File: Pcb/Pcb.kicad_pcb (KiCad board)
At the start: 2 copper layers, 152.3 x 104.7 mm, 133 parts, among them J1 TRRS, Q1 2N7002, SW1 SW_Push, SW10 SW_Push, SW11 SW_Push, SW12 SW_Push, SW13 SW_Push, SW14 SW_Push, SW15 SW_Push, SW16 SW_Push, SW17 SW_Push, SW18 SW_Push, SW19 SW_Push, SW2 SW2, SW20 SW_Push, SW21 SW_Push, SW22 SW_Push, SW23 SW_Push, SW24 SW_Push, SW25 SW_Push, SW26 SW_Push, SW27 SW_Push, SW28 SW_Push, SW29 SW_Push, SW3 SW_Push, SW4 SW_Push, SW5 SW_Push, SW6 SW_Push, SW7 SW_Push, SW8 SW_Push, SW9 SW_Push, U1 ProMicro

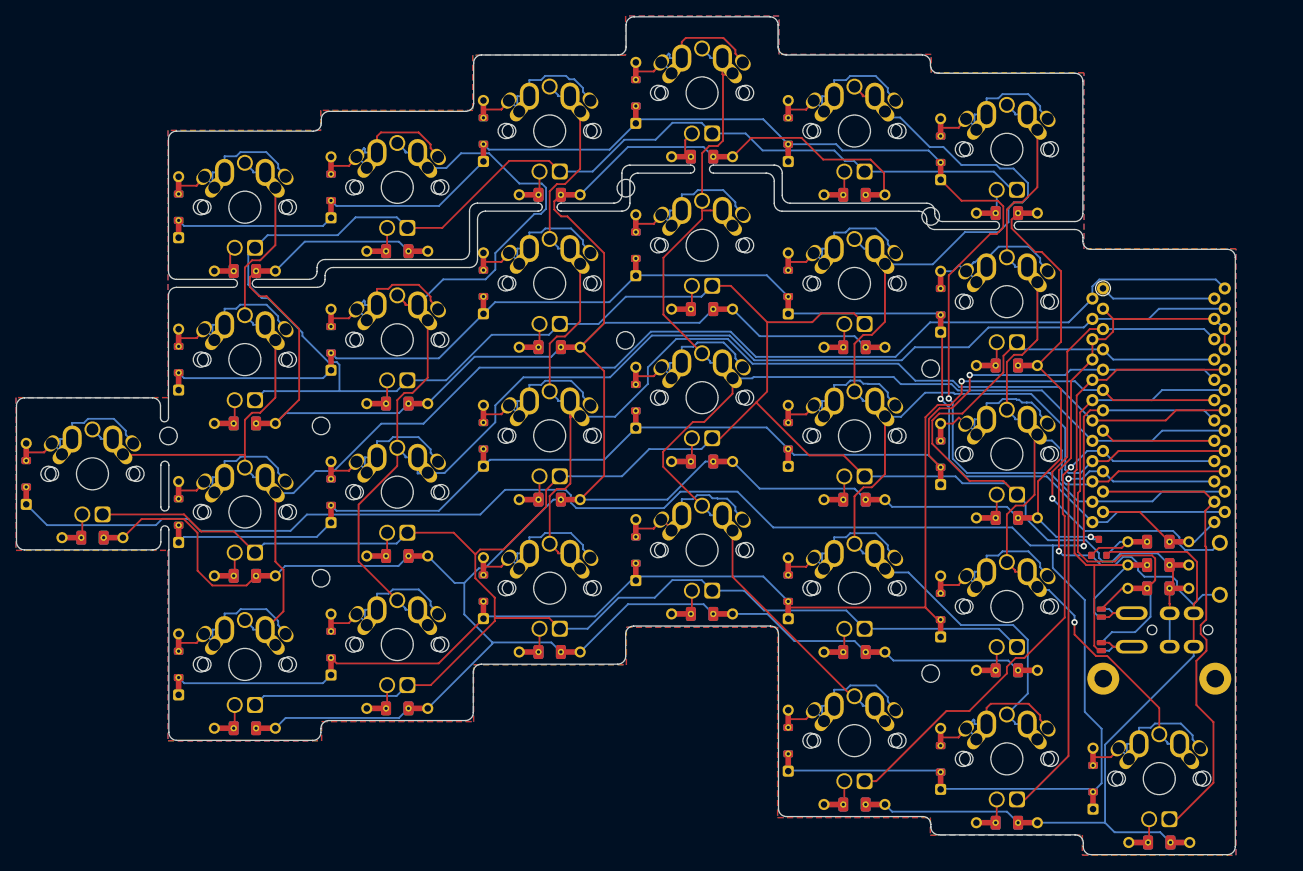
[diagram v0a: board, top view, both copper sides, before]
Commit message: Delete all tracks
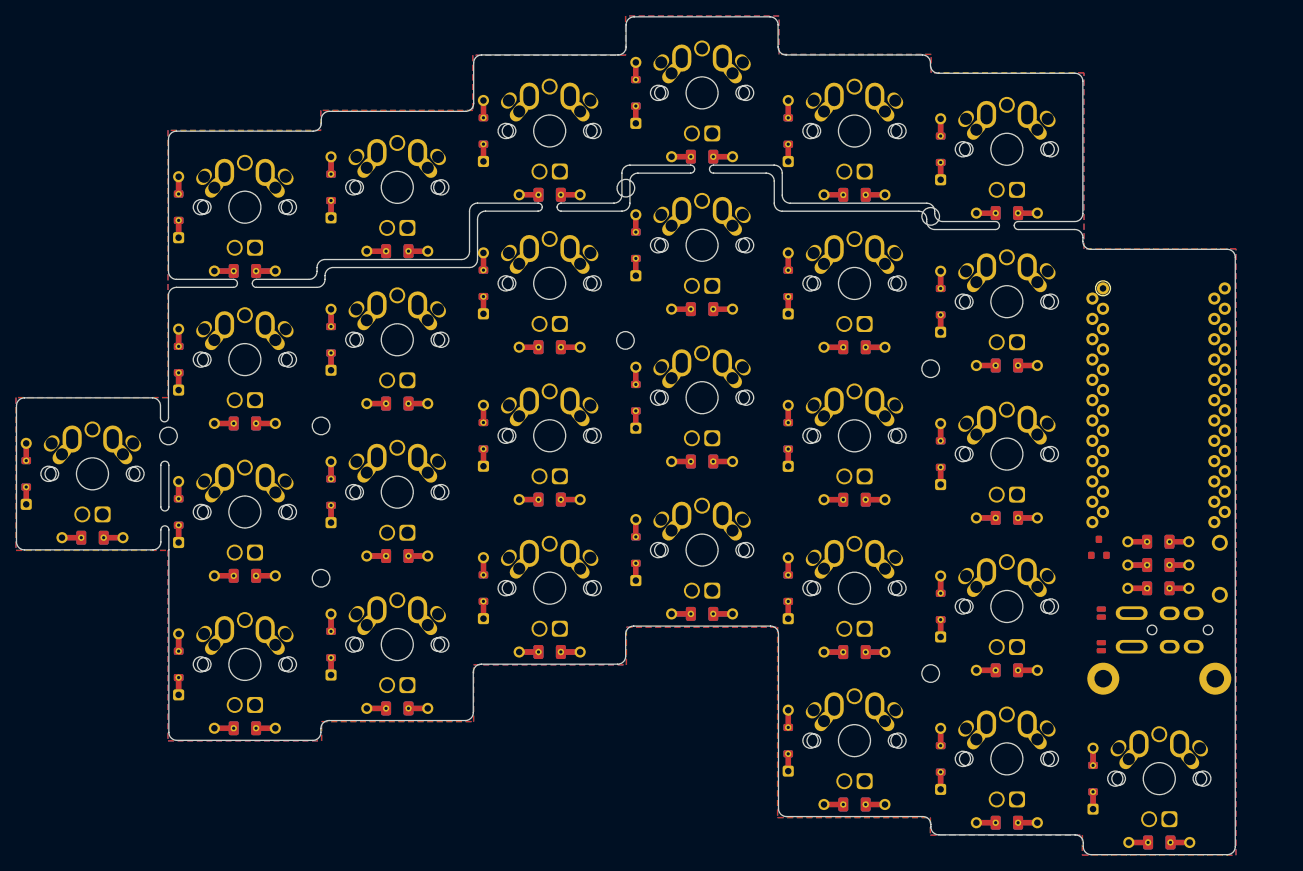
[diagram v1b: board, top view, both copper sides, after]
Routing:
- net VCC: track 572.4 -> 0.00 mm
- net /LEDOut: track 543.6 -> 0.00 mm, vias 1 -> 0
- net /rowE: track 255.7 -> 0.00 mm, vias 1 -> 0
- net /col0: track 231.3 -> 0.00 mm
- net /col1: track 218.4 -> 0.00 mm
- net /rowA: track 196.6 -> 0.00 mm, vias 1 -> 0
- net /col4: track 195.5 -> 0.00 mm
- net /col3: track 183.5 -> 0.00 mm
- net /rowD: track 179.1 -> 0.00 mm, vias 1 -> 0
- net GND: track 169.8 -> 0.00 mm, vias 1 -> 0
- net /rowB: track 169.5 -> 0.00 mm, vias 1 -> 0
- net /col2: track 167.3 -> 0.00 mm
- net /rowC: track 162.4 -> 0.00 mm, vias 1 -> 0
- net /col5: track 137.0 -> 0.00 mm, vias 1 -> 0
- net /CAPS: track 72.6 -> 0.00 mm, vias 1 -> 0
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
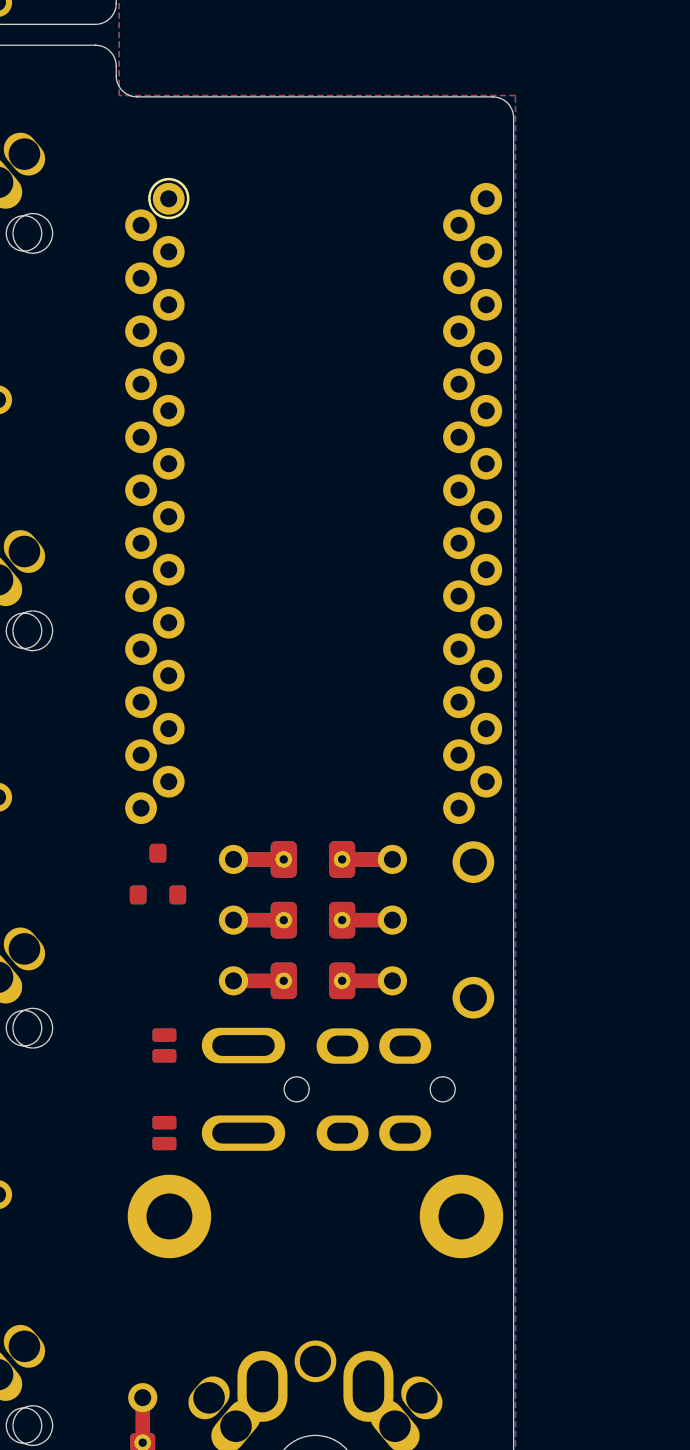
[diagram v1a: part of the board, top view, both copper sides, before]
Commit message: Remove I2C resistors
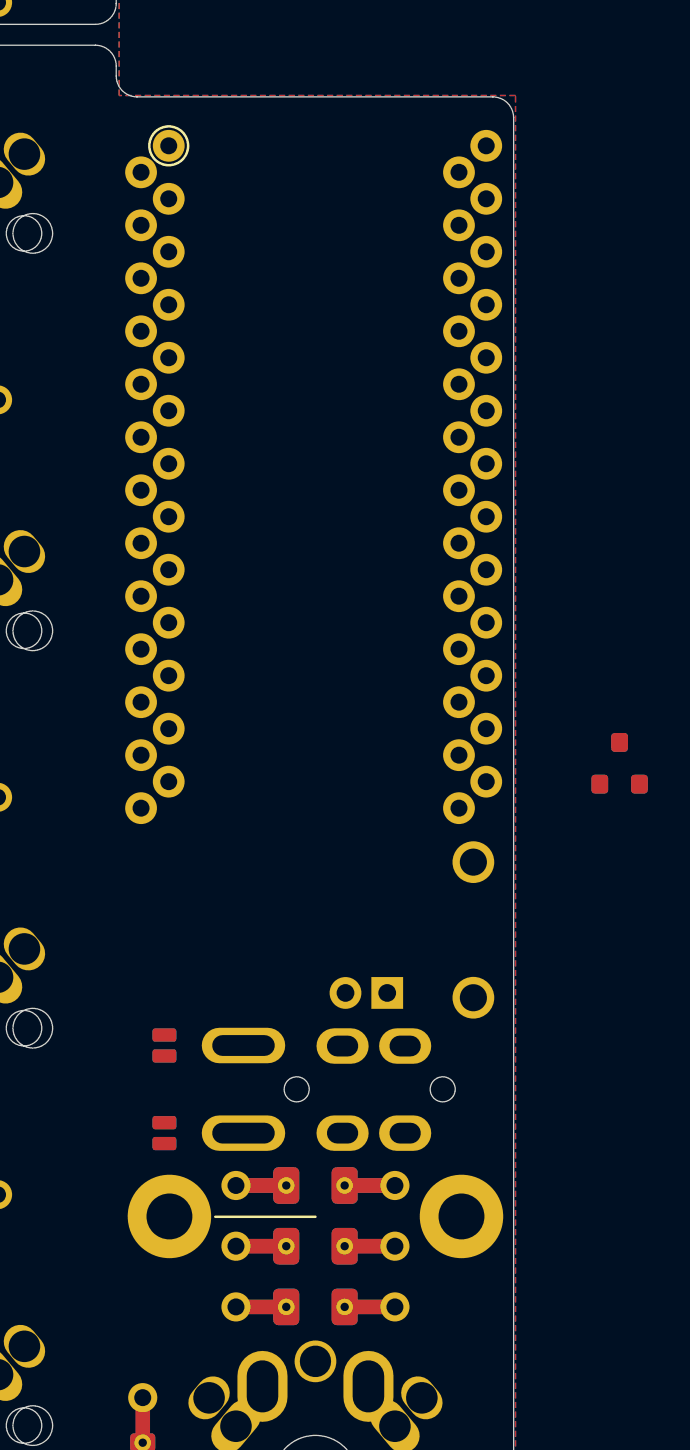
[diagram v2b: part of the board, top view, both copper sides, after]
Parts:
- added J2: JST, Used_Footprints:JST_THT_2.0, F.Cu at (222.4, 102.1)
- moved Q1 22.8 mm to (234.5, 91.2)
- moved R29 15.6 mm to (220.0, 114.3)
- moved R30 15.6 mm to (220.0, 117.2)
- moved R31 15.6 mm to (220.0, 111.3)
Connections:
- D54 pad 2: /CAPS -> VCC
- D55 pad 2: /SCROLL -> VCC
- D56 pad 2: /NUM -> VCC
- R26 pad 2: GND -> /LEDOut
- R27 pad 2: GND -> /LEDOut
- R28 pad 2: GND -> /LEDOut
- U1 pad 1: /col0 -> /B+
- U1 pad 10: /col5 -> /col4
- U1 pad 11: /rowA -> /col5
- U1 pad 12: /rowB -> /rowA
- U1 pad 13: /LED -> /rowB
- U1 pad 14: /NUM -> /LED
- U1 pad 15: /SCROLL -> Net-(U1-Pad15)
- U1 pad 16: /CAPS -> Net-(U1-Pad16)
- U1 pad 18: /rowE -> Net-(U1-Pad18)
- U1 pad 19: /rowD -> /rowE
- U1 pad 2: /col1 -> /col0
- U1 pad 20: /rowC -> /rowD
- U1 pad 21: VCC -> /rowC
- U1 pad 22: RST -> VCC
- U1 pad 23: GND -> RST
- U1 pad 24: Net-(U1-Pad24) -> GND
- U1 pad 3: GND -> /col1
- U1 pad 5: SDA -> GND
- U1 pad 6: SCL -> SDA
- U1 pad 7: /col2 -> SCL
- U1 pad 8: /col3 -> /col2
- U1 pad 9: /col4 -> /col3

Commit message: Route and fill all zones
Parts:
- removed J2: JST, Used_Footprints:JST_THT_2.0
- removed JP2, JP3, JP4, JP5: Jumper, 1symblos:Jumper
- removed R29: 4.7, Used_Footprints:Resistor_Hybrid_1205
- removed R30: 4.7k, Used_Footprints:Resistor_Hybrid_1205
- moved Q1 13.1 mm to (223.3, 97.9), turned to 180 degrees
- moved R31 9.70 mm to (219.1, 101.7)
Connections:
- J1 pad A: Net-(J1-PadA) -> /SDA
- J1 pad B: GND -> VCC
- J1 pad C: VCC -> Net-(J1-PadC)
- J1 pad D: Net-(J1-PadD) -> GND
- U1 pad 1: /B+ -> /col0
- U1 pad 10: /col4 -> /col5
- U1 pad 11: /col5 -> /rowA
- U1 pad 12: /rowA -> /rowB
- U1 pad 13: /rowB -> /LED
- U1 pad 14: /LED -> Net-(U1-Pad14)
- U1 pad 18: Net-(U1-Pad18) -> /rowE
- U1 pad 19: /rowE -> /rowD
- U1 pad 2: /col0 -> /col1
- U1 pad 20: /rowD -> /rowC
- U1 pad 21: /rowC -> VCC
- U1 pad 22: VCC -> RST
- U1 pad 23: RST -> GND
- U1 pad 24: GND -> Net-(U1-Pad24)
- U1 pad 3: /col1 -> GND
- U1 pad 5: GND -> /SDA
- U1 pad 6: SDA -> Net-(U1-Pad6)
- U1 pad 7: SCL -> /col2
- U1 pad 8: /col2 -> /col3
- U1 pad 9: /col3 -> /col4
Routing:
- net /LEDOut: track 0.00 -> 623.9 mm, vias 0 -> 2
- net VCC: track 0.00 -> 618.2 mm
- net /rowE: track 0.00 -> 259.5 mm, vias 0 -> 2
- net /col4: track 0.00 -> 253.2 mm, vias 0 -> 4
- net /col0: track 0.00 -> 250.3 mm
- net /col1: track 0.00 -> 200.2 mm
- net /rowA: track 0.00 -> 183.6 mm, vias 0 -> 3
- net /rowB: track 0.00 -> 176.9 mm
- net /col3: track 0.00 -> 174.8 mm, vias 0 -> 2
- net /rowD: track 0.00 -> 171.8 mm, vias 0 -> 1
- net /col2: track 0.00 -> 167.7 mm, vias 0 -> 1
- net /rowC: track 0.00 -> 158.8 mm
- net /col5: track 0.00 -> 135.8 mm
- net GND: track 0.00 -> 82.9 mm
- net /SDA: track 0.00 -> 47.9 mm, vias 0 -> 1
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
